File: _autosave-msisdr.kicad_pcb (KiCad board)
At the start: 2 copper layers, 46.3 x 90.7 mm, 84 parts, among them J1 VCC_GPIO, J10 SMA_VHF1, J11 USB_OTG, J12 Conn_01x02, J2 GPIO0, J3 GPIO1, J4 GPIO2, J5 GPIO3, J6 SMA_0_30MHZ, J7 SMA_30_60MHZ, J8 SMA_VHF2, J9 SMA_UHF, U1 msi2500, U2 msi001, U3 RT9193-28, U4 AP7313-30SAG, Y1 24MHz, Y2 24MHZ

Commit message: Added an U.FL male socket for L Band antanae
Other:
- rule pad_to_mask_clearance: 0.2 -> 0
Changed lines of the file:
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@@
     (pad_size 4.064 4.064)
     (pad_drill 3)
-    (pad_to_mask_clearance 0.2)
+    (pad_to_mask_clearance 0)
     (aux_axis_origin 0 0)
     (visible_elements 7FFEFFFF)
@@
       (drillshape 0)
       (scaleselection 1)
-      (outputdirectory "gerberv2/"))
+      (outputdirectory "gerberv3/"))
   )
   (net 0 "")

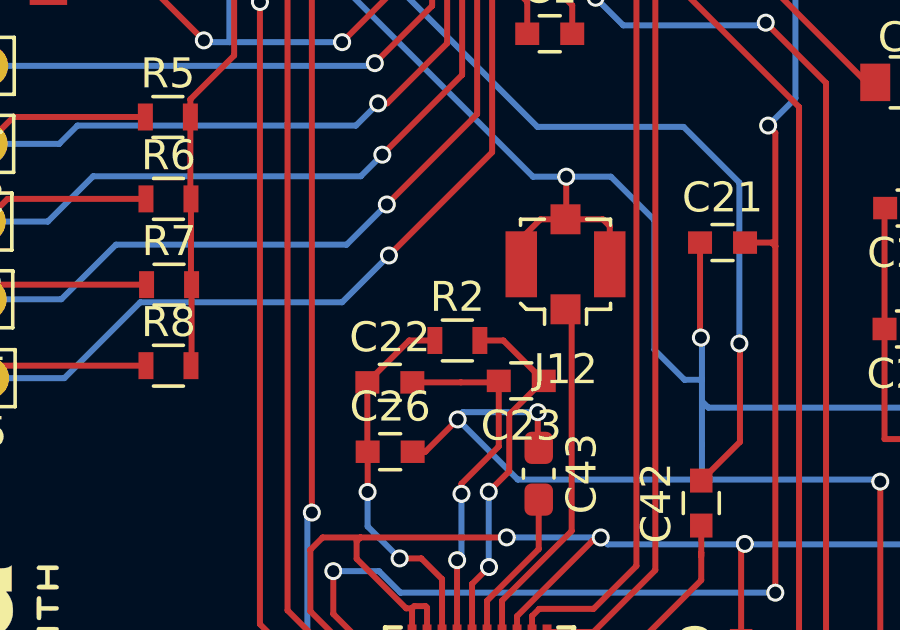
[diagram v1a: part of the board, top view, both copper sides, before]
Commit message: Fixed clearance issue
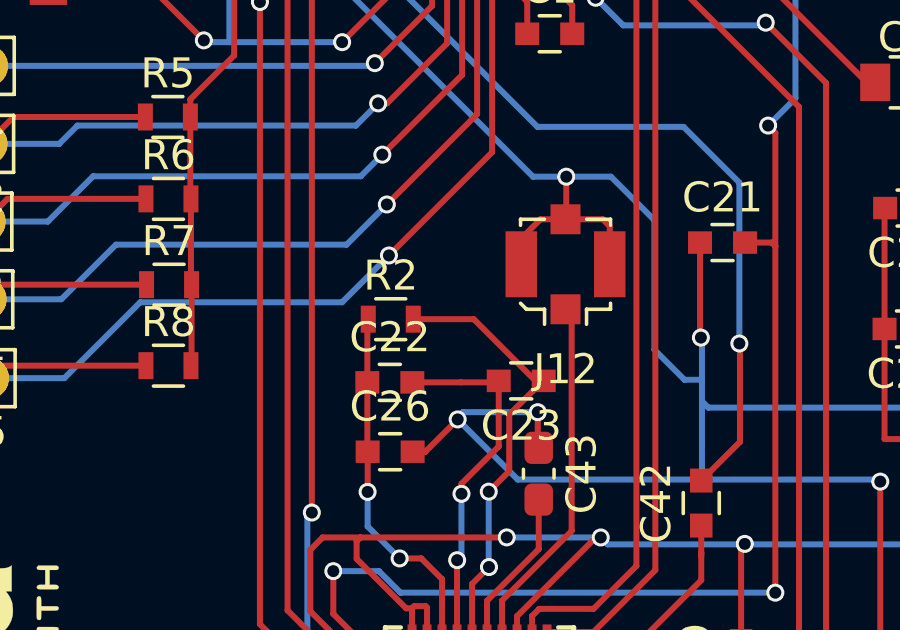
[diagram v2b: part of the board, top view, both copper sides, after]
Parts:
- moved R2 2.33 mm to (132.4, 92.0)
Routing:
- net Net-(C23-Pad1): track 12.1 -> 14.6 mm
- net Net-(C22-Pad1): track 12.6 -> 11.9 mm
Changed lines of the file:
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@@
     (thickness 1.6)
     (drawings 7)
-    (tracks 974)
+    (tracks 975)
     (zones 0)
     (modules 84)
@@
       (drillshape 0)
       (scaleselection 1)
-      (outputdirectory "gerberv3/"))
+      (outputdirectory "gerberv4/"))
   )
   (net 0 "")
@@
   )
   (module Resistors_SMD:R_0603 (layer F.Cu)
-    (at 134.62 92.71)
+    (at 132.4 92)
     (descr "Resistor SMD 0603, reflow soldering, Vishay (see dcrcw.pdf)")
     (tags "resistor 0603")
@@
   (segment (start 131.619 94.106) (end 131.619 96.40768) (width 0.2) (layer F.Cu) (net 14))
   (segment (start 131.619 96.40768) (end 131.62972 96.4184) (width 0.2) (layer F.Cu) (net 14))
-  (segment (start 133.015 92.71) (end 131.619 94.106) (width 0.2) (layer F.Cu) (net 14))
-  (segment (start 133.87 92.71) (end 133.015 92.71) (width 0.2) (layer F.Cu) (net 14))
+  (segment (start 131.619 92.031) (end 131.65 92) (width 0.2) (layer F.Cu) (net 14))
+  (segment (start 131.619 94.106) (end 131.619 92.031) (width 0.2) (layer F.Cu) (net 14))
   (segment (start 132.97 57.22) (end 132.97 55.64) (width 0.2) (layer F.Cu) (net 15))
   (segment (start 133.93 54.68) (end 136.019 54.68) (width 0.2) (layer F.Cu) (net 15))
@@
   (segment (start 136.34901 95.18099) (end 136.34901 97.06683) (width 0.2) (layer F.Cu) (net 44))
   (segment (start 137.499 94.056) (end 137.474 94.056) (width 0.2) (layer F.Cu) (net 44))
-  (segment (start 136.153 92.71) (end 137.499 94.056) (width 0.2) (layer F.Cu) (net 44))
-  (segment (start 135.37 92.71) (end 136.153 92.71) (width 0.2) (layer F.Cu) (net 44))
+  (segment (start 137.224002 94.056) (end 137.499 94.056) (width 0.2) (layer F.Cu) (net 44))
+  (segment (start 135.168002 92) (end 137.224002 94.056) (width 0.2) (layer F.Cu) (net 44))
+  (segment (start 133.15 92) (end 135.168002 92) (width 0.2) (layer F.Cu) (net 44))
   (segment (start 131.22148 125.82582) (end 135.16102 125.82582) (width 0.2) (layer F.Cu) (net 45))
   (segment (start 135.16102 125.82582) (end 135.38454 125.6023) (width 0.2) (layer F.Cu) (net 45))
